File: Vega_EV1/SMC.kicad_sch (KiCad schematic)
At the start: 41 parts, among them J16 ATX-24, J21 ISP, J25 PS2 Pwr Src, J26 Front Panel, J6 Ext. NMI, J7 RTC GPIO, Q1 2N7000, Q2 2N7000, SW1 FSM4JH, SW2 FSM4JH, SW3 FSM4JH, U12 ATtiny861-20P, U13 MCP7940N-xP, Y1 ECS-.327-6-13X

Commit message: Fix #16, widen transistor footprints
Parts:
- Q1, Q2: footprint Package_TO_SOT_THT:TO-92_Inline -> Package_TO_SOT_THT:TO-92_Inline_Wide
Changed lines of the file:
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@@
 			)
 		)
-		(property "Footprint" "Package_TO_SOT_THT:TO-92_Inline"
+		(property "Footprint" "Package_TO_SOT_THT:TO-92_Inline_Wide"
 			(at 130.302 176.276 0)
 			(effects
@@
 			)
 		)
-		(property "Footprint" "Package_TO_SOT_THT:TO-92_Inline"
+		(property "Footprint" "Package_TO_SOT_THT:TO-92_Inline_Wide"
 			(at 129.54 151.384 0)
 			(effects

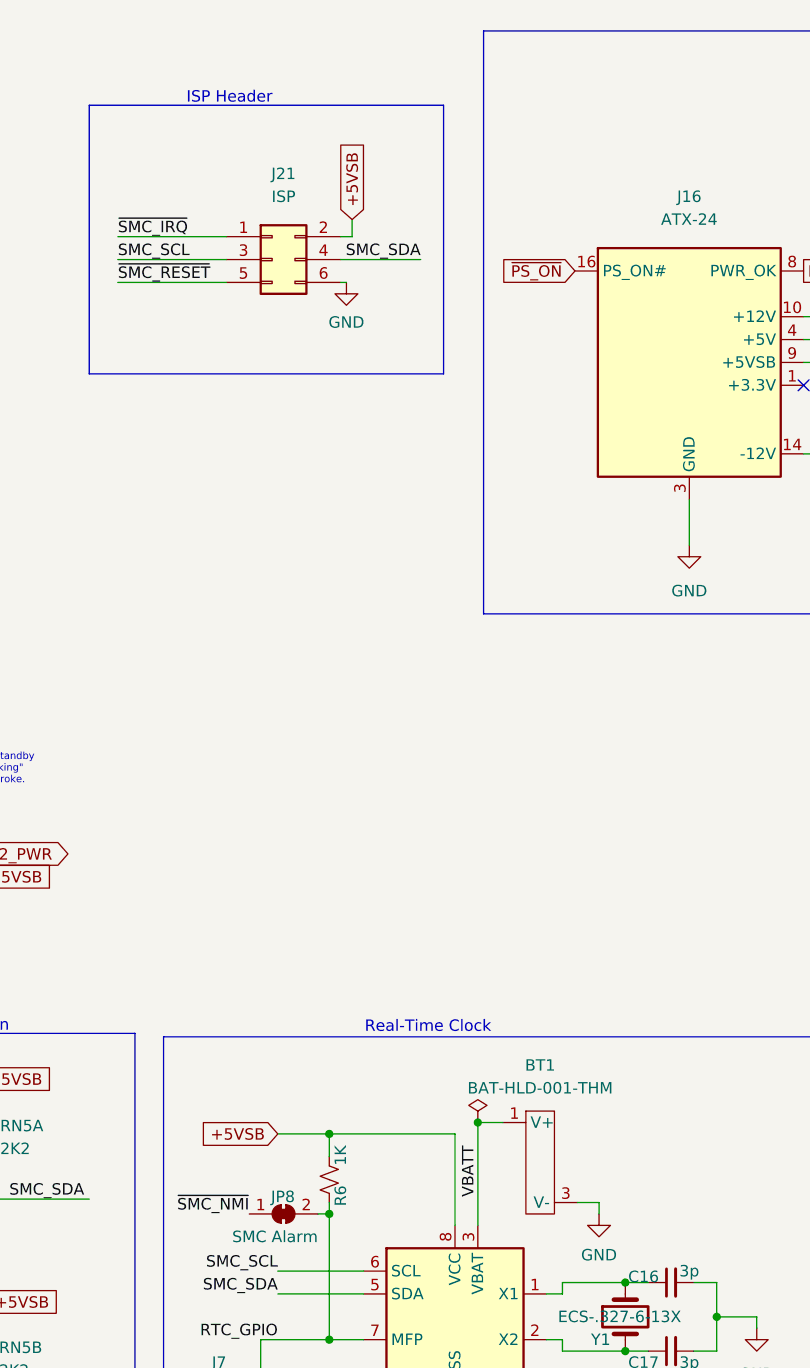
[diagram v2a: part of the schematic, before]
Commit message: More space between Edge and YM2151 Add IEC logic back in IDC headers for NES and IEC
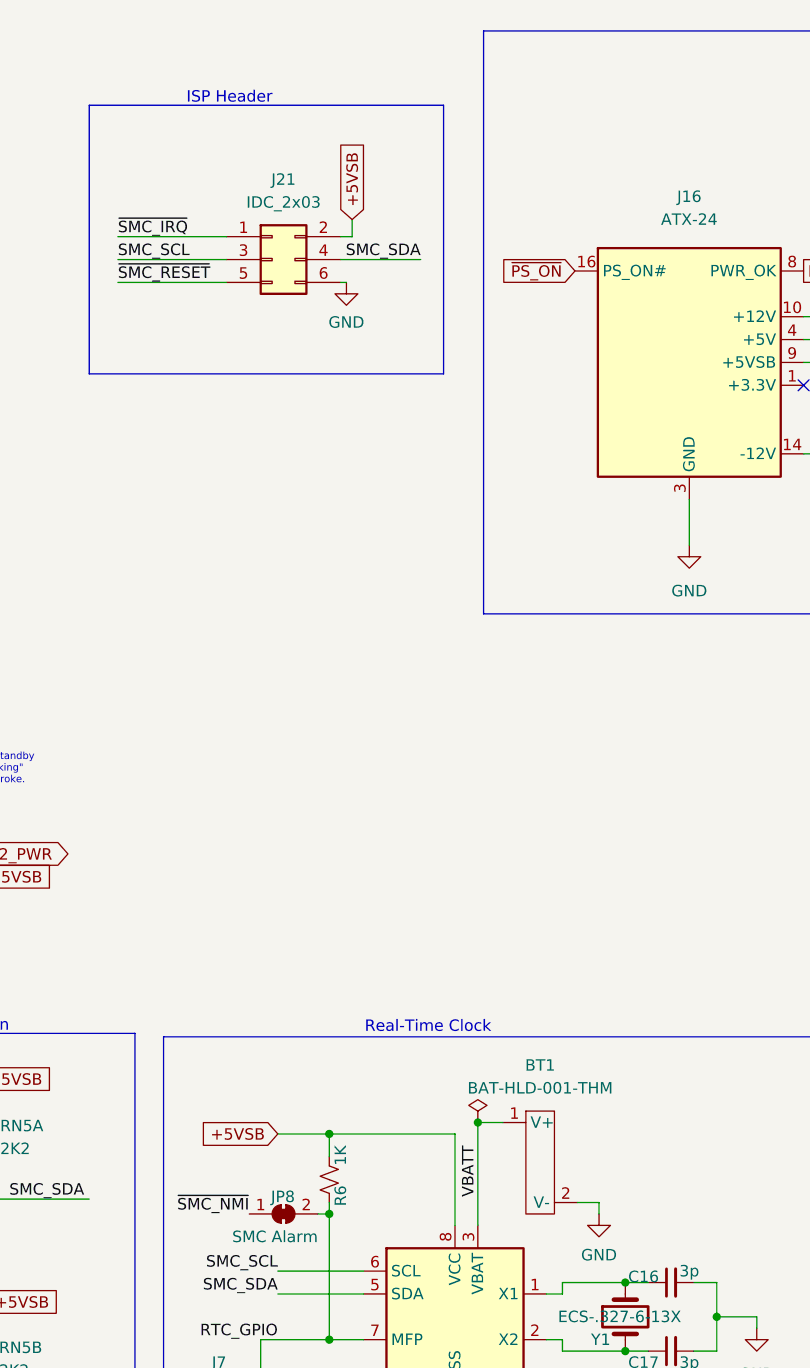
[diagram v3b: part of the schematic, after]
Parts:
- BT1: footprint OtterX:CELL_BATT_CLIP -> OtterX:AliEx_BatClip
- D14: footprint Diode_THT:D_DO-35_SOD27_P7.62mm_Horizontal -> Diode_THT:D_DO-34_SOD68_P7.62mm_Horizontal
- J21: value ISP -> IDC_2x03
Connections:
- net GND: now also BT1.2 (V-); no longer BT1.3 (V-)
- net VBATT: no longer BT1.2 (V+)
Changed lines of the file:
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@@
 	(label "PS2K_CLK"
 		(at 57.15 161.29 0)
-		(fields_autoplaced yes)
 		(effects
 			(font
@@
 	(label "SMC_SCL"
 		(at 172.72 156.845 180)
-		(fields_autoplaced yes)
 		(effects
 			(font
@@
 	(label "~{SMC_IRQ}"
 		(at 154.94 41.91 0)
-		(fields_autoplaced yes)
 		(effects
 			(font
@@
 	(label "ACTLED"
 		(at 78.74 50.8 0)
-		(fields_autoplaced yes)
 		(effects
 			(font
@@
 	(label "~{SMC_RESET}"
 		(at 154.94 46.99 0)
-		(fields_autoplaced yes)
 		(effects
 			(font
@@
 	(label "SMC_SCL"
 		(at 144.272 173.736 0)
-		(fields_autoplaced yes)
 		(effects
 			(font
@@
 	(label "RESBTN_PD"
 		(at 107.95 68.58 0)
-		(fields_autoplaced yes)
 		(effects
 			(font
@@
 	(label "BI_ACTLED"
 		(at 111.76 50.8 0)
-		(fields_autoplaced yes)
 		(effects
 			(font
@@
 	(label "SMC_SDA"
 		(at 78.74 58.42 0)
-		(fields_autoplaced yes)
 		(effects
 			(font
@@
 	(label "~{SMC_IRQ}"
 		(at 57.15 156.21 0)
-		(fields_autoplaced yes)
 		(effects
 			(font
@@
 	(label "SMC_SDA"
 		(at 172.72 159.385 180)
-		(fields_autoplaced yes)
 		(effects
 			(font
@@
 	(label "PS2K_DAT"
 		(at 57.15 163.83 0)
-		(fields_autoplaced yes)
 		(effects
 			(font
@@
 	(label "PS2M_DAT"
 		(at 57.15 166.37 0)
-		(fields_autoplaced yes)
 		(effects
 			(font
@@
 	(label "FP_PWRLED"
 		(at 78.74 102.87 0)
-		(fields_autoplaced yes)
 		(effects
 			(font
@@
 	(label "FP_ACTLED"
 		(at 55.245 102.87 0)
-		(fields_autoplaced yes)
 		(effects
 			(font
@@
 	(label "PWR_OK"
 		(at 78.74 43.18 0)
-		(fields_autoplaced yes)
 		(effects
 			(font
@@
 	(label "PS2M_CLK"
 		(at 57.15 168.91 0)
-		(fields_autoplaced yes)
 		(effects
 			(font
@@
 	(label "POW_PD"
 		(at 107.95 45.72 0)
-		(fields_autoplaced yes)
 		(effects
 			(font
@@
 	(label "~{RES}"
 		(at 57.15 158.75 0)
-		(fields_autoplaced yes)
 		(effects
 			(font
@@
 	(label "12V0_UF"
 		(at 233.045 50.8 0)
-		(fields_autoplaced yes)
 		(effects
 			(font
@@
 	(label "PS2K_DAT"
 		(at 78.74 66.04 0)
-		(fields_autoplaced yes)
 		(effects
 			(font
@@
 	(label "PS2K_CLK"
 		(at 78.74 40.64 0)
-		(fields_autoplaced yes)
 		(effects
 			(font
@@
 	(label "RES_BTN"
 		(at 58.42 107.95 0)
-		(fields_autoplaced yes)
 		(effects
 			(font
@@
 	(label "5V0_UF"
 		(at 233.045 53.34 0)
-		(fields_autoplaced yes)
 		(effects
 			(font
@@
 	(label "SMC_SDA"
 		(at 142.875 148.844 0)
-		(fields_autoplaced yes)
 		(effects
 			(font
@@
 	(label "ACTLED"
 		(at 38.735 102.87 0)
-		(fields_autoplaced yes)
 		(effects
 			(font
@@
 	(label "~{SMC_RESET}"
 		(at 78.74 76.2 0)
-		(fields_autoplaced yes)
 		(effects
 			(font
@@
 	(label "SMC_SCL"
 		(at 78.74 63.5 0)
-		(fields_autoplaced yes)
 		(effects
 			(font
@@
 	(label "RTC_GPIO"
 		(at 172.72 164.465 180)
-		(fields_autoplaced yes)
 		(effects
 			(font
@@
 	(label "N12V0_UF"
 		(at 233.045 66.04 0)
-		(fields_autoplaced yes)
 		(effects
 			(font
@@
 	(label "~{SMC_NMI}"
 		(at 78.74 38.1 0)
-		(fields_autoplaced yes)
 		(effects
 			(font
@@
 	(label "PS2M_DAT"
 		(at 78.74 71.12 0)
-		(fields_autoplaced yes)
 		(effects
 			(font
@@
 	(label "SMC_SDA"
 		(at 188.595 44.45 180)
-		(fields_autoplaced yes)
 		(effects
 			(font
@@
 	(label "PS2M_CLK"
 		(at 78.74 73.66 0)
-		(fields_autoplaced yes)
 		(effects
 			(font
@@
 	(label "~{PS_ON}"
 		(at 78.74 48.26 0)
-		(fields_autoplaced yes)
 		(effects
 			(font
@@
 	(label "~{SMC_NMI}"
 		(at 169.545 150.495 180)
-		(fields_autoplaced yes)
 		(effects
 			(font
@@
 	(label "POW_BTN"
 		(at 78.74 45.72 0)
-		(fields_autoplaced yes)
 		(effects
 			(font
@@
 	(label "RESBTN_PD"
 		(at 55.245 110.49 0)
-		(fields_autoplaced yes)
 		(effects
 			(font
@@
 	(label "5VSB_UF"
 		(at 233.045 55.88 0)
-		(fields_autoplaced yes)
 		(effects
 			(font
@@
 	(label "SMC_SCL"
 		(at 154.94 44.45 0)
-		(fields_autoplaced yes)
 		(effects
 			(font
@@
 	(label "~{SMC_IRQ}"
 		(at 78.74 60.96 0)
-		(fields_autoplaced yes)
 		(effects
 			(font
@@
 	(label "POW_BTN"
 		(at 86.995 107.95 180)
-		(fields_autoplaced yes)
 		(effects
 			(font
@@
 	(label "RES_BTN"
 		(at 78.74 68.58 0)
-		(fields_autoplaced yes)
 		(effects
 			(font
@@
 	(label "NMI_BTN"
 		(at 80.01 55.88 0)
-		(fields_autoplaced yes)
 		(effects
 			(font
@@
 	(label "VBATT"
 		(at 194.945 148.59 90)
-		(fields_autoplaced yes)
 		(effects
 			(font
@@
 	(label "~{RES}"
 		(at 78.74 35.56 0)
-		(fields_autoplaced yes)
 		(effects
 			(font
@@
 	(label "POW_PD"
 		(at 86.995 110.49 180)
-		(fields_autoplaced yes)
 		(effects
 			(font
@@
 			)
 		)
-		(property "Footprint" "Diode_THT:D_DO-35_SOD27_P7.62mm_Horizontal"
+		(property "Footprint" "Diode_THT:D_DO-34_SOD68_P7.62mm_Horizontal"
 			(at 97.79 38.1 0)
 			(effects
@@
 		(fields_autoplaced yes)
 		(property "Reference" "J21"
-			(at 173.355 34.925 0)
+			(at 173.355 35.56 0)
 			(effects
 				(font
@@
 			)
 		)
-		(property "Value" "ISP"
-			(at 173.355 37.465 0)
+		(property "Value" "IDC_2x03"
+			(at 173.355 38.1 0)
 			(effects
 				(font
@@
 			)
 		)
-		(property "Footprint" "OtterX:CELL_BATT_CLIP"
+		(property "Footprint" "OtterX:AliEx_BatClip"
 			(at 197.739 142.24 0)
 			(effects
@@
 		(pin "1"
 		)
-		(pin "3"
-		)
 		(pin "2"
